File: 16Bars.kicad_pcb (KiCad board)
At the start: 2 copper layers, 28.5 x 105 mm, 36 parts, among them IC1 CD4033BE, IC2 CD4033BE, IC3 CD4510BE, J1 CLOCK_IN, J2 Conn_02x05_Odd_Even, Q1 2N3904, Q2 2N3904, Q3 2N3904, Q4 2N3904, Q5 2N3904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

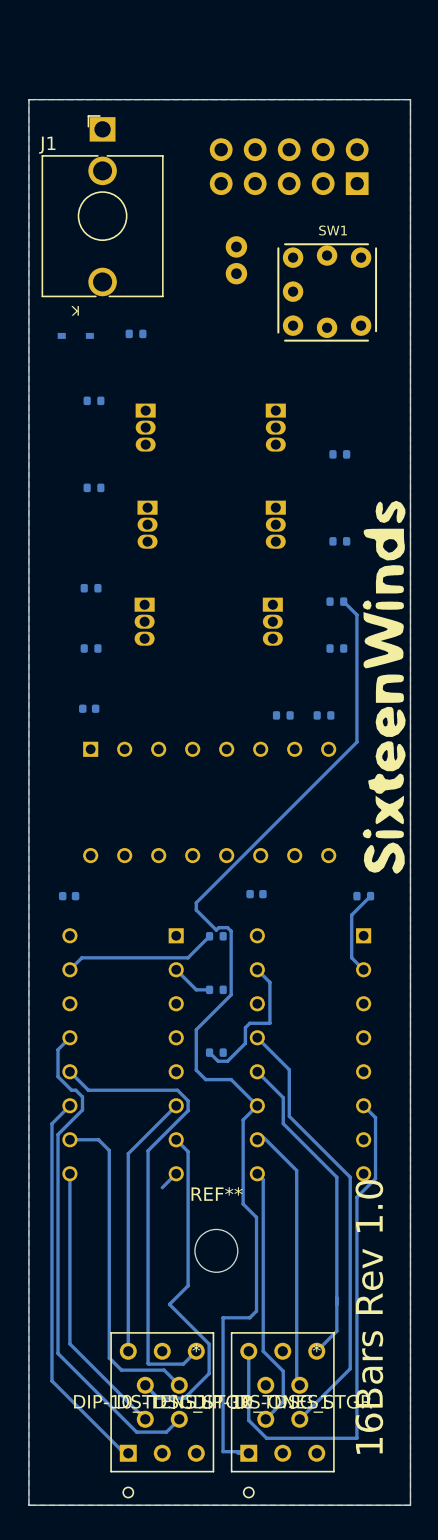
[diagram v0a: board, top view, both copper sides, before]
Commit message: Update PCB and Schematic Footprints
Better 7Seg layout
Update 7seg footprint
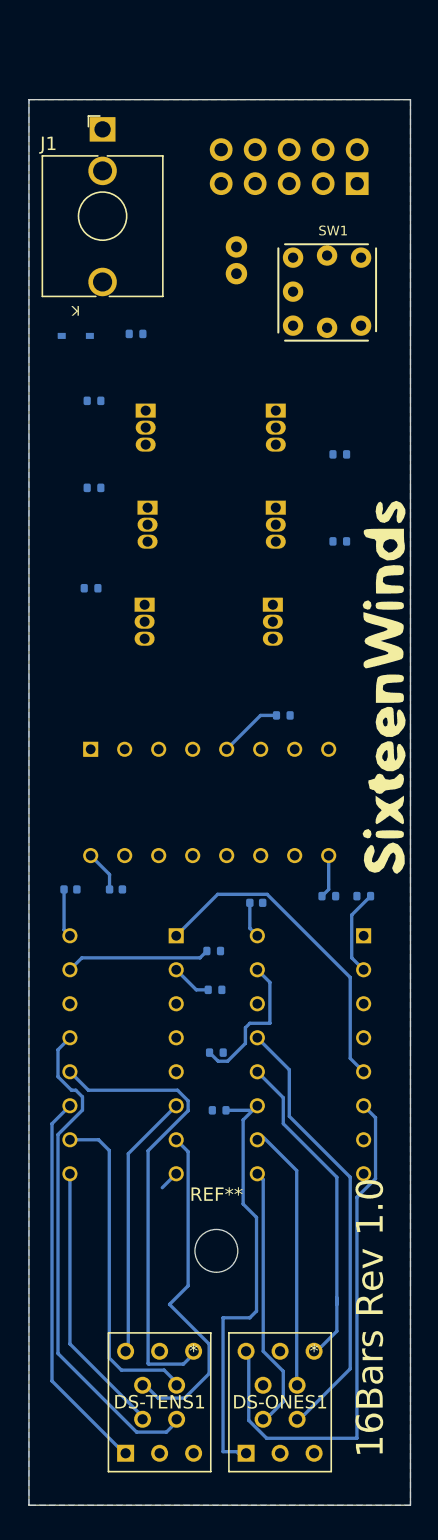
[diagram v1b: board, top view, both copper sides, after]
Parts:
- removed R12, R15: R, Resistor_SMD:R_0402_1005Metric
- moved R11 39.0 mm to (70.7, 110.5)
- moved C2 13.6 mm to (63.0, 94.0)
- moved R6 13.5 mm to (78.9, 94.5)
- moved R4 1.12 mm to (70.3, 98.6)
- moved C4 0.65 mm to (73.5, 95.0)
- moved C3 0.51 mm to (59.6, 94.0)
- moved DS-ONES1 0.20 mm to (77.8, 128.5)
- moved DS-TENS1 0.20 mm to (68.8, 128.5)
- moved R3 0.10 mm to (70.4, 101.5)
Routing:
- net /E1: track 80.8 -> 34.3 mm
- net CARRY_1: track 0.00 -> 24.3 mm
- net +12V: track 0.00 -> 9.45 mm
- net Net-(IC3-Pad5): track 0.00 -> 4.77 mm
- net 16_BARS_RESET: track 22.5 -> 25.1 mm

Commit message: Add PowerLED. Add ThonkButton Symbol and Footprint
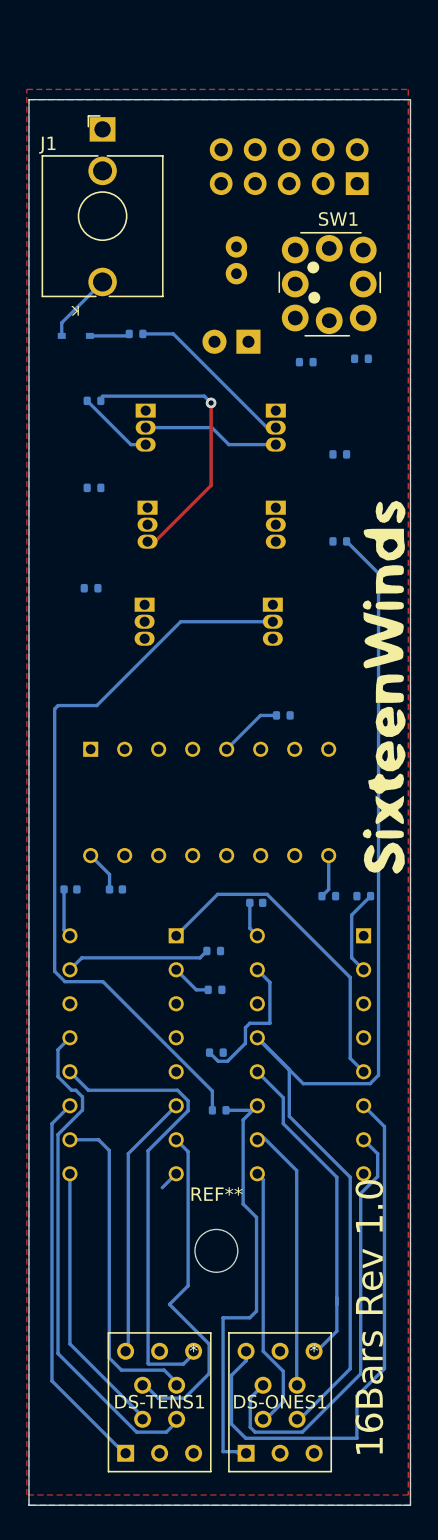
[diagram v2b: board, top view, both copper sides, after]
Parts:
- added D2: LED, LED_THT:LED_D3.0mm, B.Cu at (72.9, 53.1)
- added R12: 2K, Resistor_SMD:R_0402_1005Metric, B.Cu at (77.2, 54.6)
- added R15: 2K, Resistor_SMD:R_0402_1005Metric, B.Cu at (81.3, 54.4)
- DS-ONES1, DS-TENS1: value DIP-10_TDSG_STGR -> TDSR0760
- R10, R11, R13, R14: value R -> 10K
- R2: value RESET_PD -> 10K
- SW1: value RESET_CLOCK_LED -> SW_Push_LED_Thonk_Low_Profile; footprint Button_Switch_THT:Thonk-LED-Button-MomentaryON -> TDSR*:ThonkLowProfileButton
- moved SW1 2.79 mm to (78.9, 46.1)
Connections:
- C1 pad 1: +12V -> 16_BARS_RESET
- C2 pad 1: +12V -> 16_BARS_RESET
- C3 pad 2: +12V -> 16_BARS_RESET
- C4 pad 2: +12V -> 16_BARS_RESET
- IC1 pad 16: +12V -> 16_BARS_RESET
- IC2 pad 16: +12V -> 16_BARS_RESET
- IC3 pad 10: +12V -> 16_BARS_RESET
- IC3 pad 16: +12V -> 16_BARS_RESET
- IC3 pad 9: 16_BARS_RESET -> RESET
- J2 pad 1: +12V -> 16_BARS_RESET
- J2 pad 2: +12V -> 16_BARS_RESET
- Q1 pad 1: GND -> CLOCK_IN
- Q1 pad 3: CLOCK_IN -> Net-(Q1-Pad3)
- Q2 pad 1: GND -> Net-(Q2-Pad1)
- Q3 pad 3: +12V -> 16_BARS_RESET
- Q4 pad 1: /DISP-IC1-6 -> GND
- Q5 pad 3: +12V -> 16_BARS_RESET
- Q6 pad 1: 16_BARS_RESET -> GND
- R13 pad 1: /DISP-IC1-6 -> 16_BARS_RESET
- R6 pad 2: 16_BARS_RESET -> RESET
- R7 pad 1: +12V -> 16_BARS_RESET
- R8 pad 1: +12V -> 16_BARS_RESET
- R8 pad 2: CLOCK_IN -> Net-(Q1-Pad3)
- SW1 pad 1: +12V -> 16_BARS_RESET
- SW1 pad 2: 16_BARS_RESET -> unconnected-(SW1-Pad2)
- SW1 pad 3: GND -> RESET
- SW1 pad 4: Net-(Q2-Pad3) -> unconnected-(SW1-Pad4)
- SW1 pad L1: (no net) -> Net-(Q2-Pad1)
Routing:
- net Net-(Q4-Pad2): track 0.00 -> 55.5 mm
- net /C1: track 32.9 -> 84.5 mm
- net /G1: track 0.00 -> 32.2 mm
- net 16_BARS_RESET: track 25.1 -> 52.3 mm, vias 0 -> 1
- net Net-(Q1-Pad2): track 0.00 -> 12.8 mm
- net CLOCK_IN: track 0.00 -> 10.2 mm
- net +12V: track 9.45 -> 0.00 mm
- net Net-(Q2-Pad3): track 0.00 -> 5.72 mm
- net Net-(D1-Pad2): track 0.00 -> 5.29 mm
- net RESET: track 0.00 -> 3.24 mm
- net Net-(D1-Pad1): track 0.00 -> 3.00 mm
- net /F1: track 39.6 -> 42.0 mm
- added copper zone on F.Cu, net 16_BARS_RESET

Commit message: Complete Surface Mount Version
Fix 16BarsReset Label by adding resistor
Add TODOs for clock and bar division switches
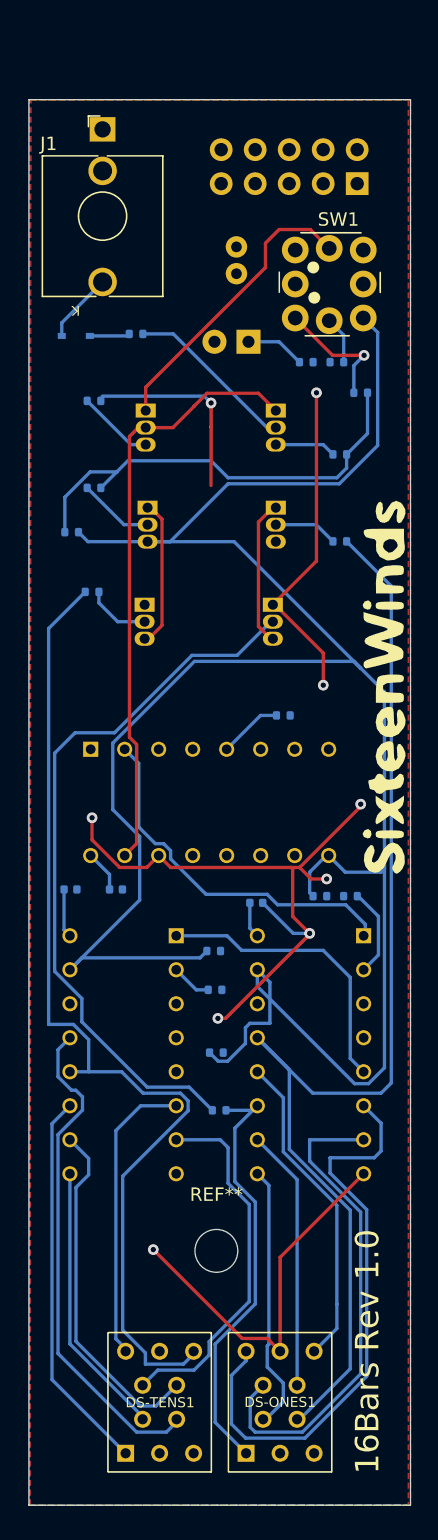
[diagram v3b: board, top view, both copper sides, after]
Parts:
- added R16: 10K, Resistor_SMD:R_0402_1005Metric, B.Cu at (81.3, 56.9)
- added R17: 10K, Resistor_SMD:R_0402_1005Metric, B.Cu at (59.7, 67.3)
- R1: value CLK_INHB_PD -> 10K
- R7: value 1K -> 10K
- moved R15 1.85 mm to (79.5, 54.6), turned to 0 degrees
- moved R1 0.99 mm to (80.5, 94.5)
- moved R6 0.67 mm to (78.2, 94.5)
- moved R14 0.28 mm to (61.2, 71.8), turned to 0 degrees
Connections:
- C1 pad 1: 16_BARS_RESET -> +12V
- C2 pad 1: 16_BARS_RESET -> +12V
- C3 pad 2: 16_BARS_RESET -> +12V
- C4 pad 2: 16_BARS_RESET -> +12V
- D2 pad 2: 16_BARS_RESET -> +12V
- IC1 pad 15: 16_BARS_RESET -> /16_BARS_RESET
- IC1 pad 16: 16_BARS_RESET -> +12V
- IC2 pad 15: 16_BARS_RESET -> /16_BARS_RESET
- IC2 pad 16: 16_BARS_RESET -> +12V
- IC3 pad 10: 16_BARS_RESET -> +12V
- IC3 pad 16: 16_BARS_RESET -> +12V
- IC3 pad 9: RESET -> /16_BARS_RESET
- J2 pad 1: 16_BARS_RESET -> +12V
- J2 pad 2: 16_BARS_RESET -> +12V
- Q3 pad 3: 16_BARS_RESET -> +12V
- Q5 pad 3: 16_BARS_RESET -> /16_BARS_RESET
- R13 pad 1: 16_BARS_RESET -> +12V
- R2 pad 2: 16_BARS_RESET -> /16_BARS_RESET
- R4 pad 2: 16_BARS_RESET -> /16_BARS_RESET
- R6 pad 2: RESET -> /16_BARS_RESET
- R7 pad 1: 16_BARS_RESET -> +12V
- R8 pad 1: 16_BARS_RESET -> +12V
- SW1 pad 1: 16_BARS_RESET -> unconnected-(SW1-Pad1)
- SW1 pad 2: unconnected-(SW1-Pad2) -> Net-(SW1-Pad2)
- SW1 pad 3: RESET -> unconnected-(SW1-Pad3)
- SW1 pad 4: unconnected-(SW1-Pad4) -> /16_BARS_RESET
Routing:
- net /16_BARS_RESET: track 0.00 -> 172.1 mm
- net GND: track 1.47 -> 100.6 mm, vias 0 -> 8
- net +12V: track 0.00 -> 61.8 mm, vias 0 -> 1
- net 16_BARS_RESET: track 52.3 -> 0.00 mm, vias 1 -> 0
- net /B2: track 34.6 -> 75.6 mm
- net CLOCK_IN: track 10.2 -> 44.7 mm
- net CLOCK_BAR: track 0.00 -> 27.4 mm
- net Net-(Q2-Pad1): track 0.00 -> 22.0 mm
- net Net-(Q5-Pad1): track 0.00 -> 11.1 mm
- net Net-(Q3-Pad1): track 0.00 -> 11.0 mm
- net Net-(SW1-Pad2): track 0.00 -> 9.41 mm, vias 0 -> 1
- net Net-(Q5-Pad2): track 0.00 -> 5.65 mm
- net Net-(Q6-Pad2): track 0.00 -> 4.82 mm
- net Net-(Q3-Pad2): track 0.00 -> 4.79 mm
- net /G1: track 32.2 -> 36.8 mm
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- added copper zone on F.Cu, net +12V
- removed copper zone on F.Cu, net 16_BARS_RESET

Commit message: SMD Transistors and LED
Move fabrication files to Fabrication dir
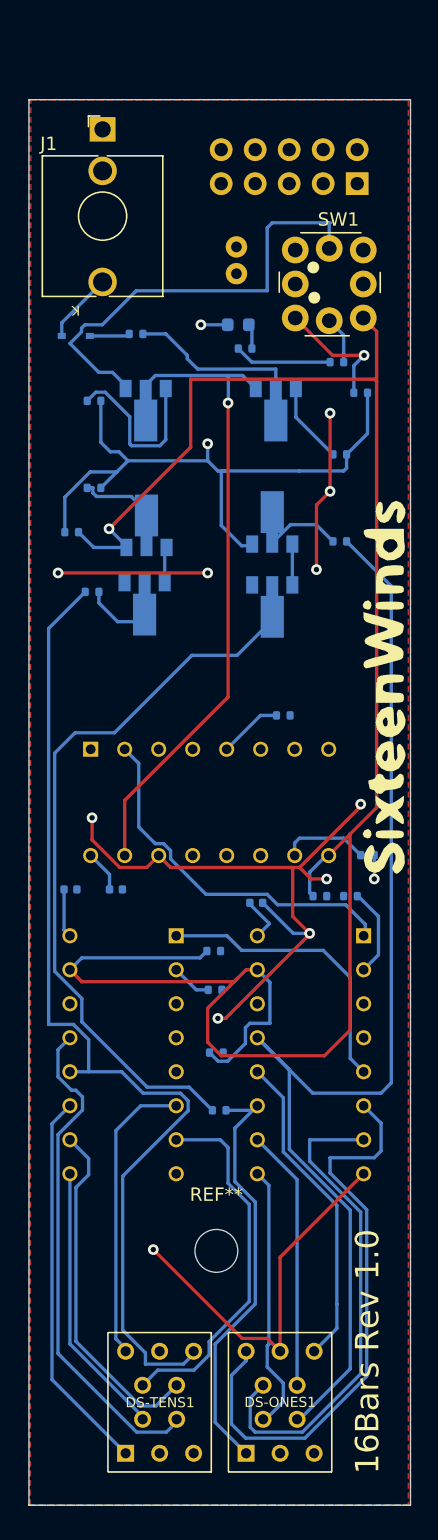
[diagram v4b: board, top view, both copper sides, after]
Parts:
- added R18: 10K, Resistor_SMD:R_0402_1005Metric, B.Cu at (81.8, 91.4)
- D2: footprint LED_THT:LED_D3.0mm -> LED_SMD:LED_0603_1608Metric
- Q1, Q2, Q3, Q4, Q5, Q6: footprint Package_TO_SOT_THT:TO-92_Inline -> Package_TO_SOT_SMD:SOT-89-3
- moved R12 4.68 mm to (72.6, 53.6), turned to 0 degrees
- moved D2 1.48 mm to (72.1, 51.8)
- moved Q5 1.32 mm to (65.3, 66.8), turned to 90 degrees
- moved Q3 1.10 mm to (74.7, 66.5), turned to 90 degrees
- moved Q4 0.17 mm to (74.7, 72.9)
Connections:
- IC3 pad 10: +12V -> Net-(IC3-Pad10)
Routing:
- net /16_BARS_RESET: track 172.1 -> 148.4 mm, vias 0 -> 1
- net Net-(Q2-Pad1): track 22.0 -> 33.7 mm
- net Net-(Q5-Pad1): track 11.1 -> 2.69 mm
- net Net-(Q3-Pad1): track 11.0 -> 3.05 mm
- net Net-(Q2-Pad3): track 5.72 -> 13.0 mm
- net Net-(IC3-Pad10): track 0.00 -> 6.54 mm
- net GND: track 100.6 -> 106.3 mm, vias 8 -> 11
- net CLOCK_IN: track 44.7 -> 48.3 mm, vias 0 -> 1
- net Net-(R11-Pad2): track 53.8 -> 57.1 mm
- net Net-(Q1-Pad2): track 12.8 -> 15.5 mm
- net Net-(D2-Pad1): track 4.44 -> 1.87 mm
- net Net-(Q1-Pad3): track 4.57 -> 6.07 mm
- net Net-(Q3-Pad2): track 4.79 -> 5.62 mm
- net Net-(Q5-Pad2): track 5.65 -> 6.39 mm
- net +12V: track 61.8 -> 61.4 mm, vias 1 -> 3

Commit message: LCSC Part Numbers
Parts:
- Q5: value 2N3904 -> NPN BJT
- R8: value 10k -> 10K
